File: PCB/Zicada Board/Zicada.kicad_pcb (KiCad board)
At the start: 2 copper layers, 57.4 x 12 mm, 60 parts, among them J1 Conn_ARM_JTAG_SWD_10, J2 Conn_01x01_Pin, J3 Conn_01x01_Pin, SW1 SW_Push, U1 nRF52840, U2 HDC2080, U3 SM351LT, U4 TPS610981, U5 OPT3001, Y1 32MHz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

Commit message: Everything 0402, 4 layer board
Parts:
- added C101: 100n,16V, Passives:C0402, F.Cu at (154.0, 89.3)
- C1, C4: footprint Capacitor_SMD:C_0603_1608Metric -> Passives:C0402
- C10, C13, C14, C16, C19, C20, C21, C22, C24: value 100nF -> 100n,16V; footprint Capacitor_SMD:C_0603_1608Metric -> Passives:C0402
- C11: value 4.7uF -> 10u,6.3V
- C12, C2: value 1uF -> 1u,10V; footprint Capacitor_SMD:C_0603_1608Metric -> Passives:C0402
- C15, C17, C5, C6: value 12pF -> 12p,50V; footprint Capacitor_SMD:C_0603_1608Metric -> Passives:C0402
- C18, C23: value 10uF -> 10u,6.3V
- C3: value 820pF -> 820p,50V; footprint Capacitor_SMD:C_0603_1608Metric -> Passives:C0402
- C7: value 0.5pF -> 0.5p,50V; footprint Capacitor_SMD:C_0603_1608Metric -> Passives:C0402
- C8: value 100pF -> 100p,50V; footprint Capacitor_SMD:C_0603_1608Metric -> Passives:C0402
- C9: value 0.8pF -> 0.8p,50V; footprint Capacitor_SMD:C_0603_1608Metric -> Passives:C0402
- FID1, FID2, FID3, FID4: footprint Fiducial:Fiducial_1mm_Mask2mm -> Mechanical:FIDUCIAL_1mm
- J1: footprint Connector_PinHeader_1.27mm:PinHeader_2x05_P1.27mm_Vertical_SMD -> Connector:TC2050-IDC-NLFP
- L1: footprint Inductor_SMD:L_0603_1608Metric -> Passives:L0402
- R1, R2, R3, R5, R6, R7, R8: footprint Resistor_SMD:R_0603_1608Metric -> Passives:R0402
- moved FID1 9.21 mm to (163.1, 97.0)
- moved J1 2.82 mm to (168.8, 96.8), turned to 90 degrees
- moved C16 2.80 mm to (162.5, 94.5)
- moved C23 2.38 mm to (147.6, 93.0), turned to -90 degrees
- moved R2 2.32 mm to (172.7, 93.1), turned to -90 degrees
- moved C10 2.17 mm to (151.2, 94.5)
- moved C21 2.07 mm to (142.4, 95.5)
- moved C12 1.79 mm to (149.3, 93.0)
- moved C14 1.62 mm to (161.2, 95.8), turned to 0 degrees
- moved FID4 1.54 mm to (171.1, 96.6)
- moved C13 1.50 mm to (150.5, 93.0)
- moved R8 1.30 mm to (136.1, 90.2)
- moved C3 1.10 mm to (161.9, 91.0)
- moved C2 1.05 mm to (151.1, 91.5), turned to 180 degrees
- moved C5 0.95 mm to (152.4, 88.3), turned to 90 degrees
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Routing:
- net VDD: track 71.8 -> 32.7 mm, vias 5 -> 13
- net GND: track 62.2 -> 86.3 mm, vias 56 -> 77
- net Net-(J2-Pin_1): track 13.2 -> 19.1 mm, vias 1 -> 2
- net /NRST: track 22.1 -> 19.8 mm
- net /DEC1: track 3.65 -> 1.66 mm
- net /DEC4_6: track 12.1 -> 10.1 mm
- net Net-(U1-XL2/P0.01): track 7.52 -> 5.64 mm
- net Net-(U1-XC2): track 9.99 -> 11.6 mm
- net /VSENS: track 21.0 -> 19.4 mm, vias 0 -> 2
- net Net-(U1-XC1): track 6.41 -> 7.97 mm
- net /DEC5: track 3.10 -> 2.25 mm
- net /SWDCLK: track 41.8 -> 42.6 mm, vias 1 -> 2
- net Net-(D2-K): track 2.96 -> 2.25 mm
- net /SDA: track 33.7 -> 34.4 mm
- net /SWDIO: track 31.8 -> 31.2 mm, vias 3 -> 2
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- added copper zone on In1.Cu, net GND
- added copper zone on In2.Cu, net VDD
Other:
- copper layers 2 -> 4
- board text added: "JLC04161H-7628"
- board text added: "Zicada Rev dbr0 David Brandt 2026-02-19"
- board text removed: "Zicada Rev 3 Maximilian Kern 12/2025"

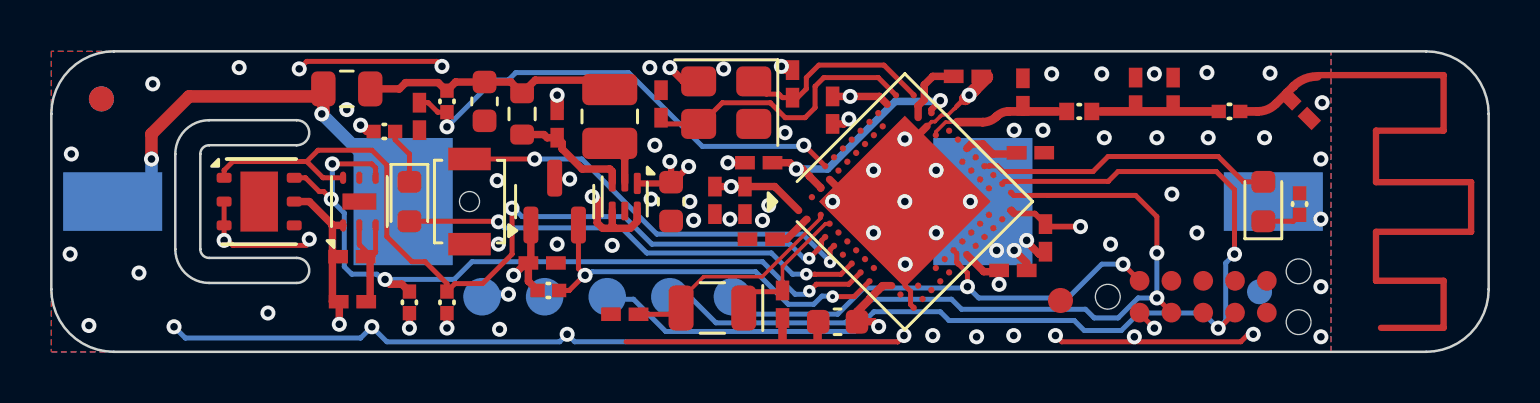
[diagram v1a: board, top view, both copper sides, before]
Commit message: Add BME688
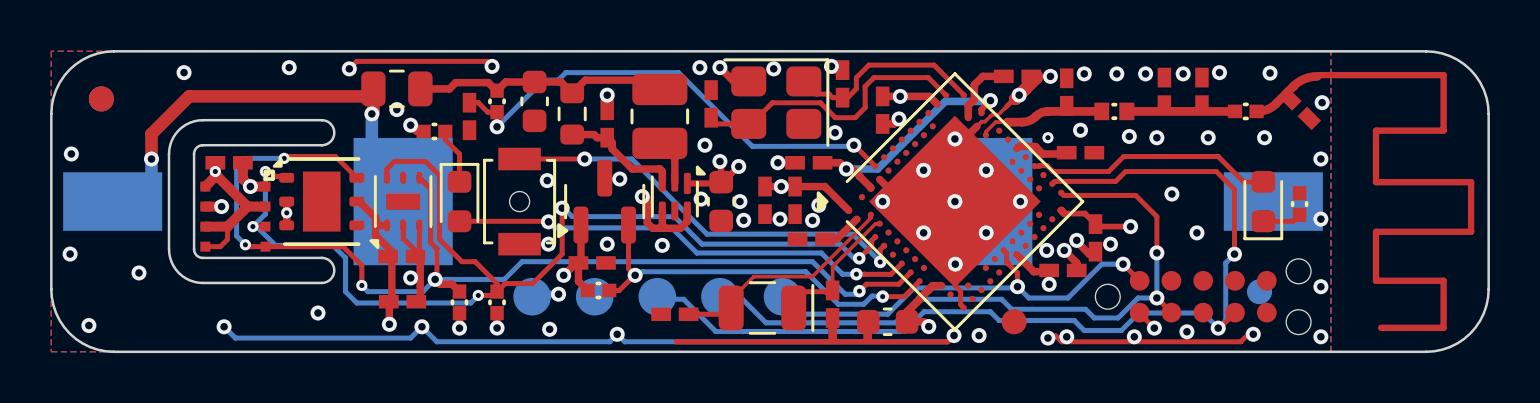
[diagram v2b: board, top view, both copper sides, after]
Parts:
- added C904: 100n,16V, Passives:C0402, F.Cu at (129.9, 91.5)
- added IC901: BME680, IC:BME680, F.Cu at (130.2, 93.6)
- moved U2 2.50 mm to (133.6, 93.0)
- moved FID1 2.04 mm to (161.2, 97.8)
- moved C10 2.00 mm to (153.2, 94.5)
- moved C101 2.00 mm to (156.0, 89.3)
- moved C11 2.00 mm to (156.2, 97.8)
- moved C12 2.00 mm to (151.3, 93.0)
- moved C13 2.00 mm to (152.5, 93.0)
- moved C14 2.00 mm to (163.2, 95.8)
- moved C15 2.00 mm to (154.0, 97.1)
- moved C16 2.00 mm to (164.5, 94.5)
- moved C17 2.00 mm to (147.7, 97.5)
- moved C18 2.00 mm to (142.1, 89.0)
- moved C19 2.00 mm to (145.0, 89.9)
- moved C2 2.00 mm to (153.1, 91.5)
- moved C20 2.00 mm to (136.8, 95.2)
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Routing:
- net VDD: track 32.7 -> 46.5 mm, vias 13 -> 14
- net /SCL: track 31.6 -> 43.3 mm, vias 4 -> 5
- net /SDA: track 34.4 -> 43.5 mm, vias 2 -> 5
- net GND: track 86.3 -> 91.9 mm, vias 77 -> 81
- net /SWDIO: track 31.2 -> 27.2 mm
- net /SWDCLK: track 42.6 -> 38.6 mm
- net /LED1: track 11.9 -> 9.90 mm
- net /NRST: track 19.8 -> 17.8 mm
- net Net-(J2-Pin_1): track 19.1 -> 20.3 mm
- net Net-(C1-Pad2): track 34.2 -> 33.5 mm
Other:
- outline, holes or cut-outs redrawn
